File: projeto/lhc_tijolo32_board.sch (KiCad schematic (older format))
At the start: 47 parts, among them J1 USB_C_Receptacle_USB2.0, J2 OLED, J3 JTAG 10pin Connector, J4 Conn_01x20_Male, Q1 MMBT3904, Q2 MMBT3904, SW1 SW_Push, SW2 SW_Push, U1 AMS1117-3.3, U2 CH340G, U3 ESP32-WROOM-32D, Y1 12MHz 10ppm, Y2 32k 20ppm

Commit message: Changed from Sparkfun to Adafruit Feather layout
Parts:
- removed B1: ESP32_THING_W_ANT_KEEPOUT, Boards:ESP32_THING, symbol SparkFun-Boards:ESP32_THING_W_ANT_KEEPOUT
- removed J1: USB_C_Receptacle_USB2.0, Connector_USB:USB_C_Receptacle_Palconn_UTC16-G, symbol Connector:USB_C_Receptacle_USB2.0
- removed J4: Conn_01x20_Male, Connector_PinHeader_2.54mm:PinHeader_1x20_P2.54mm_Vertical, symbol Connector:Conn_01x20_Male
- removed R10, R11: 0R, Resistor_SMD:R_0603_1608Metric, symbol Device:R_US
- removed R2, R3: 5k1R, Resistor_SMD:R_0603_1608Metric, symbol Device:R_US
- removed U1: AMS1117-3.3, Package_TO_SOT_SMD:SOT-223-3_TabPin2, symbol Regulator_Linear:AMS1117-3.3
- added A1: Adafruit_Feather_Generic, Module:Adafruit_Feather, symbol MCU_Module:Adafruit_Feather_Generic
- added J1: USB_A, Connector_USB:USB_A_CNCTech_1001-011-01101_Horizontal, symbol Connector:USB_A
- added J4, J5: CONN_06POLAR, MOLEX-1X6, symbol SparkFun-Connectors:CONN_06POLAR
- added U1: AP2112K-3.3, Package_TO_SOT_SMD:SOT-23-5, symbol Regulator_Linear:AP2112K-3.3
- C10: symbol Device:CP1_Small -> lhc_tijolo32_board-rescue:CP1_Small-Device
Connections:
- wire segments 252 -> 231
- no-connect marks 7 -> 5
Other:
- moved on the sheet: C9, F1

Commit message: Layout updated and added new 3d images
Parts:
- removed R12, R13: 0R, Resistor_SMD:R_0603_1608Metric, symbol Device:R_US
- added C17, C19: 100nF, Capacitor_SMD:C_0603_1608Metric, symbol Device:C_Small
- added C18: 1uF, Capacitor_SMD:C_0603_1608Metric, symbol Device:C_Small
- added U4: AP2112K-3.3, Package_TO_SOT_SMD:SOT-23-5, symbol Regulator_Linear:AP2112K-3.3
- C9: value 100nF -> 1uF
- J4, J5: footprint MOLEX-1X6 -> Connector_PinSocket_2.54mm:PinSocket_1x06_P2.54mm_Vertical
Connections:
- wire segments 231 -> 254
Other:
- moved on the sheet: C11, F1, J1, U2

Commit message: Layout updated
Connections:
- net labels removed: IO16, IO17
- wire segments 254 -> 255
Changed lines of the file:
@@
 IO15-MTDO
 Text GLabel 7950 2350 2    50   BiDi ~ 0
-IO16
+SDA
 Text GLabel 7950 2450 2    50   BiDi ~ 0
-IO17
+SCL
 Text GLabel 7950 2550 2    50   BiDi ~ 0
 IO18
@@
 Text GLabel 9400 2750 0    50   BiDi ~ 0
 IO26
-Text GLabel 9400 2850 0    50   BiDi ~ 0
+Text GLabel 10600 2150 2    50   BiDi ~ 0
 IO27
 Text GLabel 10600 1750 2    50   Input ~ 0
@@
 Wire Wire Line
 	2450 7000 2450 7100
+Wire Wire Line
+	10500 2150 10600 2150
 $EndSCHEMATC

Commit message: Layout improved
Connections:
- wire segments 255 -> 253
- no-connect marks 5 -> 7
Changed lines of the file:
@@
 Wire Notes Line
 	6350 3200 4750 3200
-Text GLabel 10600 2350 2    50   BiDi ~ 0
-IO32-32kXP
-Text GLabel 10600 2450 2    50   Input ~ 0
-IO33-32kXN
 Text GLabel 10600 2550 2    50   Input ~ 0
 IO34
@@
 Text GLabel 10600 1750 2    50   Input ~ 0
 ESP_RST
-Text GLabel 9400 2250 0    50   Input ~ 0
+Text GLabel 9400 1950 0    50   Input ~ 0
 IO21
 Text GLabel 9400 3150 0    50   Input ~ 0
@@
 Text GLabel 9400 3050 0    50   Input ~ 0
 ESP_RX
-Text GLabel 9400 2350 0    50   Input ~ 0
-IO22
+Text GLabel 9400 2050 0    50   Input ~ 0
+IO19
+Text GLabel 9800 1250 0    50   Input ~ 0
+IO23
 Text GLabel 9400 2150 0    50   Input ~ 0
-IO19
-Text GLabel 9400 2450 0    50   Input ~ 0
-IO23
-Text GLabel 9400 2050 0    50   Input ~ 0
 IO18
-Text GLabel 9400 1950 0    50   Input ~ 0
+Text GLabel 9400 2250 0    50   Input ~ 0
 IO5
 Text GLabel 9400 1750 0    50   Input ~ 0
@@
 Text GLabel 10600 2050 2    50   Input ~ 0
 ESP_BOOT
-Text GLabel 9400 1850 0    50   Input ~ 0
+Text GLabel 9400 2350 0    50   Input ~ 0
 IO4
 Text GLabel 9400 3350 0    50   Input ~ 0
@@
 	1    0    0    -1
 $EndComp
-Text GLabel 10600 2750 2    50   Input ~ 0
+Text GLabel 10600 2350 2    50   Input ~ 0
 SVP
-Text GLabel 10600 2850 2    50   Input ~ 0
+Text GLabel 10600 2450 2    50   Input ~ 0
 SVN
 $Comp
@@
 	9400 2350 9500 2350
 Wire Wire Line
-	9400 2450 9500 2450
-Wire Wire Line
 	10500 2350 10600 2350
 Wire Wire Line
@@
 	10500 2650 10600 2650
 Wire Wire Line
-	10500 2750 10600 2750
-Wire Wire Line
-	10500 2850 10600 2850
-Wire Wire Line
 	9400 2650 9500 2650
 Wire Wire Line
 	9400 2750 9500 2750
-Wire Wire Line
-	9400 2850 9500 2850
 Wire Wire Line
 	10000 3950 10000 3850
@@
 Wire Wire Line
 	10500 2150 10600 2150
+Text GLabel 9400 1850 0    50   Input ~ 0
+IO22
+Wire Wire Line
+	9800 1250 9900 1250
+Wire Wire Line
+	9900 1250 9900 1350
+NoConn ~ 9500 2450
+NoConn ~ 9500 2850
 $EndSCHEMATC

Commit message: Layout LIVE
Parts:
- JP1, JP2: footprint Jumper:SolderJumper-3_P1.3mm_Bridged12_Pad1.0x1.5mm_NumberLabels -> Jumper:SolderJumper-3_P1.3mm_Open_Pad1.0x1.5mm_NumberLabels; symbol Jumper:SolderJumper_3_Bridged12 -> Jumper:SolderJumper_3_Open
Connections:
- no-connect marks 7 -> 9
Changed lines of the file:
@@
 SDA
 $Comp
-L Jumper:SolderJumper_3_Bridged12 JP2
+L Jumper:SolderJumper_3_Open JP2
 U 1 1 5F71E23B
 P 3800 3850
 F 0 "JP2" H 3800 4055 50  0000 C CNN
 F 1 "P1" H 3800 3964 50  0000 C CNN
-F 2 "Jumper:SolderJumper-3_P1.3mm_Bridged12_Pad1.0x1.5mm_NumberLabels" H 3800 3850 50  0001 C CNN
+F 2 "Jumper:SolderJumper-3_P1.3mm_Open_Pad1.0x1.5mm_NumberLabels" H 3800 3850 50  0001 C CNN
 F 3 "~" H 3800 3850 50  0001 C CNN
 	1    3800 3850
@@
 $EndComp
 $Comp
-L Jumper:SolderJumper_3_Bridged12 JP1
+L Jumper:SolderJumper_3_Open JP1
 U 1 1 5F71F2AF
 P 3100 3850
 F 0 "JP1" H 3100 4055 50  0000 C CNN
 F 1 "P2" H 3100 3964 50  0000 C CNN
-F 2 "Jumper:SolderJumper-3_P1.3mm_Bridged12_Pad1.0x1.5mm_NumberLabels" H 3100 3850 50  0001 C CNN
+F 2 "Jumper:SolderJumper-3_P1.3mm_Open_Pad1.0x1.5mm_NumberLabels" H 3100 3850 50  0001 C CNN
 F 3 "~" H 3100 3850 50  0001 C CNN
 	1    3100 3850
@@
 Text GLabel 10600 2650 2    50   Input ~ 0
 IO35
-Text GLabel 9400 2650 0    50   BiDi ~ 0
+Text GLabel 10600 2750 2    50   BiDi ~ 0
 IO25
-Text GLabel 9400 2750 0    50   BiDi ~ 0
+Text GLabel 10600 2850 2    50   BiDi ~ 0
 IO26
 Text GLabel 10600 2150 2    50   BiDi ~ 0
@@
 	10500 2650 10600 2650
 Wire Wire Line
-	9400 2650 9500 2650
-Wire Wire Line
-	9400 2750 9500 2750
-Wire Wire Line
 	10000 3950 10000 3850
 $Comp
@@
 NoConn ~ 9500 2450
 NoConn ~ 9500 2850
+Wire Wire Line
+	10500 2750 10600 2750
+Wire Wire Line
+	10500 2850 10600 2850
+NoConn ~ 9500 2750
+NoConn ~ 9500 2650
 $EndSCHEMATC

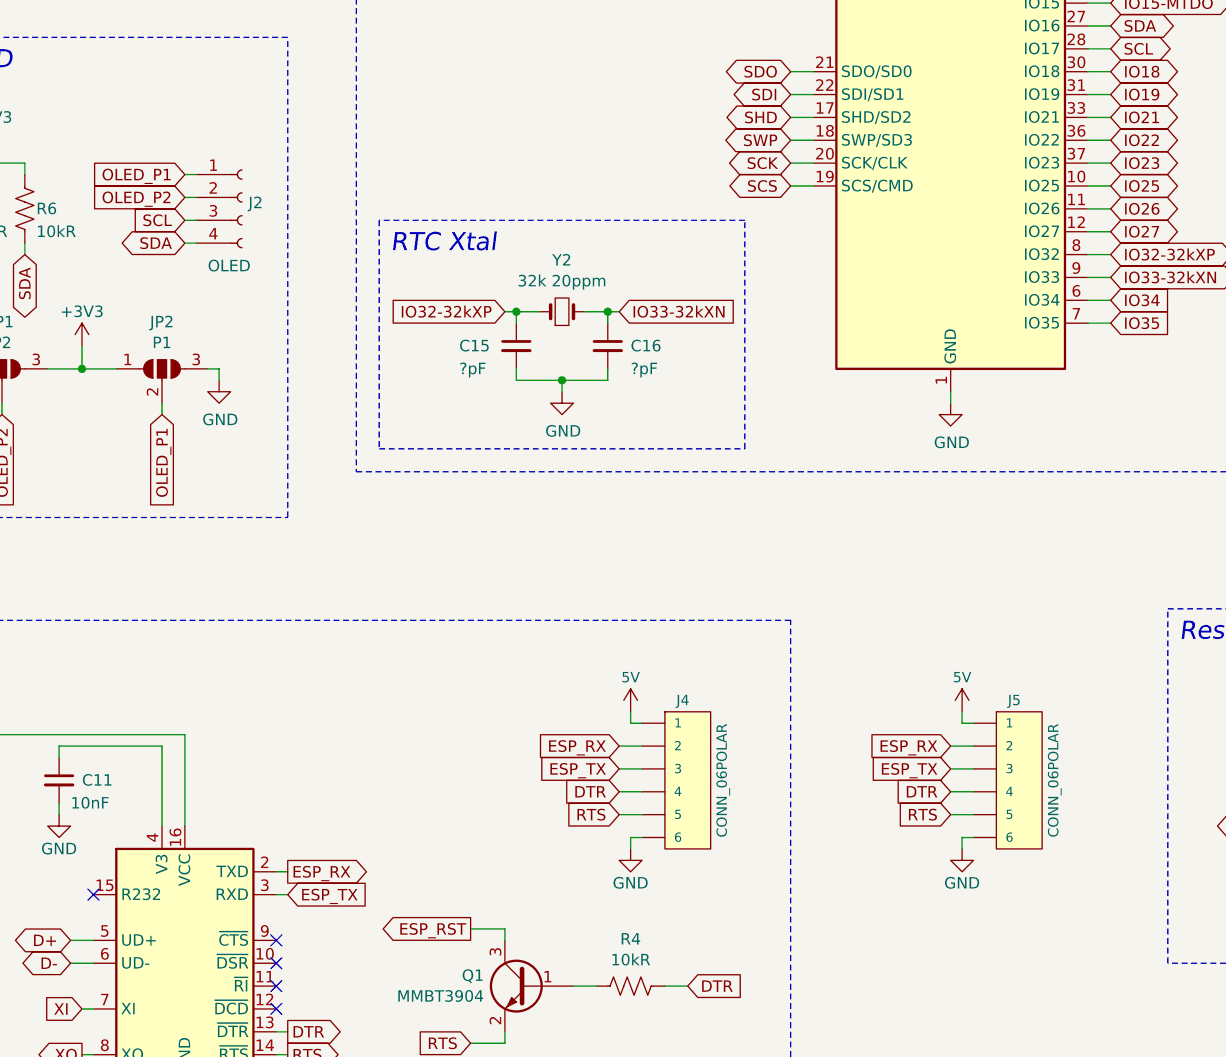
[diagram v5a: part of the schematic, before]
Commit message: Updated on some labels, footprints and symbols
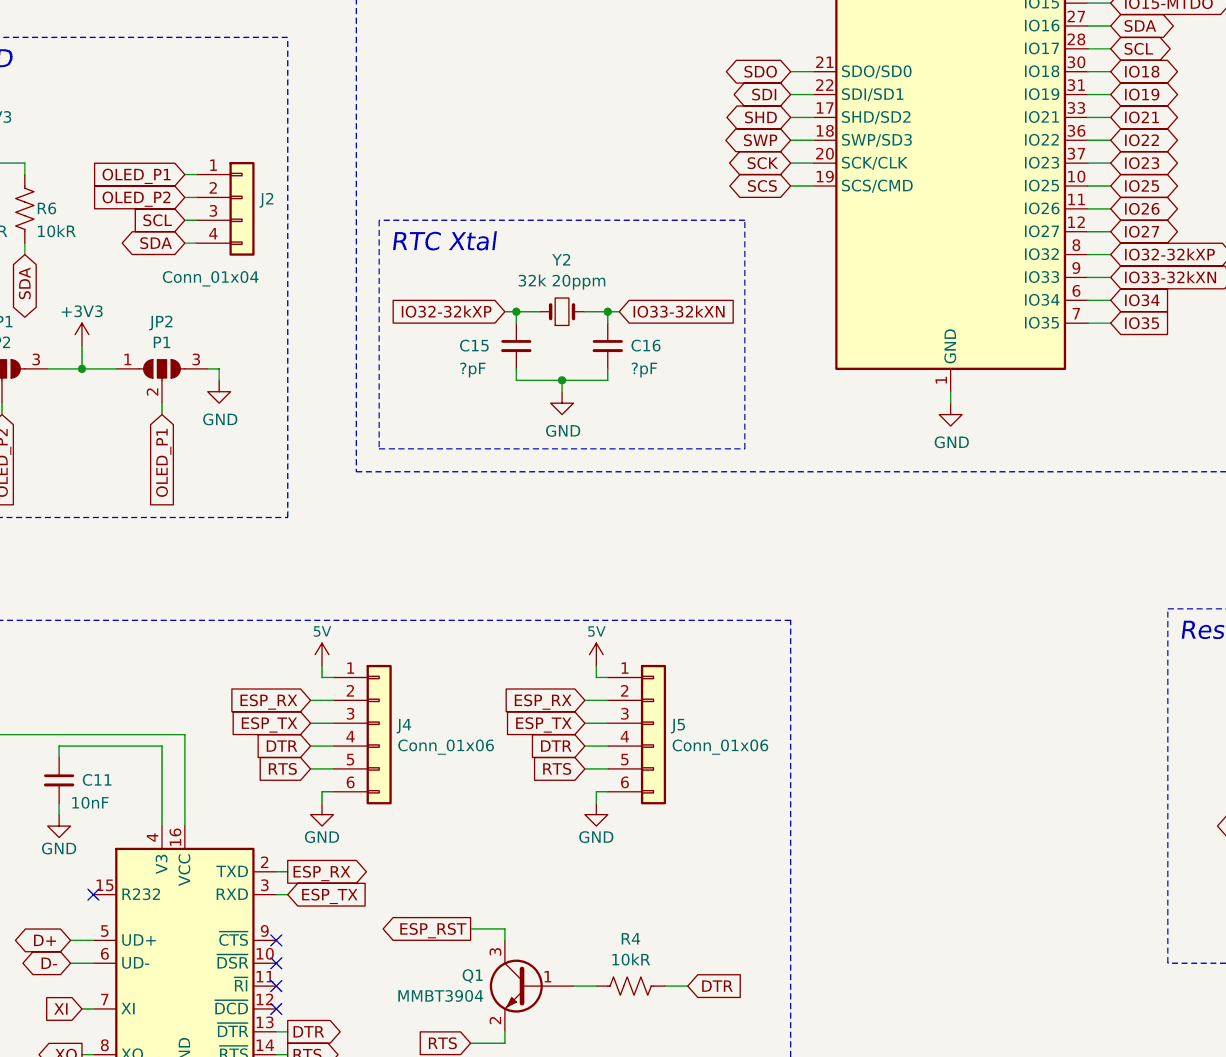
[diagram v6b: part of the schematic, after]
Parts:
- removed J2: OLED, Connector_PinHeader_2.54mm:PinHeader_1x04_P2.54mm_Vertical, symbol Connector:Conn_01x04_Female
- removed J4, J5: CONN_06POLAR, Connector_PinSocket_2.54mm:PinSocket_1x06_P2.54mm_Vertical, symbol SparkFun-Connectors:CONN_06POLAR
- added J2: Conn_01x04, Connector_PinSocket_2.54mm:PinSocket_1x04_P2.54mm_Vertical, symbol Connector_Generic:Conn_01x04
- added J4, J5: Conn_01x06, Connector_PinSocket_2.54mm:PinSocket_1x06_P2.54mm_Vertical, symbol Connector_Generic:Conn_01x06
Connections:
- net 5V: now also J4.1 (Pin_1), J5.1 (Pin_1)
- net DTR: now also J4.4 (Pin_4), J5.4 (Pin_4)
- net ESP_RX: now also J4.2 (Pin_2), J5.2 (Pin_2)
- net ESP_TX: now also J4.3 (Pin_3), J5.3 (Pin_3)
- net GND: now also J4.6 (Pin_6), J5.6 (Pin_6)
- net OLED_P1: now also J2.1 (Pin_1)
- net OLED_P2: now also J2.2 (Pin_2)
- net RTS: now also J4.5 (Pin_5), J5.5 (Pin_5)
- net SCL: now also J2.3 (Pin_3)
- net SDA: now also J2.4 (Pin_4)
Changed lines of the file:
@@
 $EndComp
 $Comp
-L Connector:Conn_01x04_Female J2
-U 1 1 5F4C7D74
-P 4150 3100
-F 0 "J2" H 4178 3076 50  0000 L CNN
-F 1 "OLED" H 4000 2800 50  0000 L CNN
-F 2 "Connector_PinHeader_2.54mm:PinHeader_1x04_P2.54mm_Vertical" H 4150 3100 50  0001 C CNN
-F 3 "~" H 4150 3100 50  0001 C CNN
-	1    4150 3100
-	1    0    0    -1
-$EndComp
-$Comp
-L SparkFun-PowerSymbols:5V #SUPPLY0101
+L lhc_tijolo32_board-rescue:5V-SparkFun-PowerSymbols #SUPPLY0101
 U 1 1 5F4CA7F8
 P 1550 6350
@@
 $EndComp
 $Comp
-L SparkFun-PowerSymbols:5V #SUPPLY0102
+L lhc_tijolo32_board-rescue:5V-SparkFun-PowerSymbols #SUPPLY0102
 U 1 1 5F4EB545
 P 1250 1050
@@
 SCL
 $Comp
-L SparkFun-PowerSymbols:5V #SUPPLY02
+L lhc_tijolo32_board-rescue:5V-SparkFun-PowerSymbols #SUPPLY02
 U 1 1 5F88471D
 P 10300 1050
@@
 	10000 3950 10000 3850
 $Comp
-L SparkFun-Connectors:CONN_06POLAR J4
-U 1 1 60537E72
-P 6000 5400
-F 0 "J4" H 5950 5300 45  0000 R CNN
-F 1 "CONN_06POLAR" V 5750 5900 45  0000 R CNN
-F 2 "Connector_PinSocket_2.54mm:PinSocket_1x06_P2.54mm_Vertical" H 6000 6100 20  0001 C CNN
-F 3 "" H 6000 5400 50  0001 C CNN
-F 4 "XXX-00000" H 5772 5734 60  0001 R CNN "Field4"
-	1    6000 5400
-	-1   0    0    1
-$EndComp
-$Comp
-L SparkFun-PowerSymbols:5V #SUPPLY0103
+L lhc_tijolo32_board-rescue:5V-SparkFun-PowerSymbols #SUPPLY0103
 U 1 1 6054C50E
-P 5850 5350
-F 0 "#SUPPLY0103" H 5900 5350 45  0001 L BNN
-F 1 "5V" H 5850 5500 45  0000 C CNN
-F 2 "XXX-00000" H 5850 5531 60  0001 C CNN
-F 3 "" H 5850 5350 60  0001 C CNN
-	1    5850 5350
+P 4500 5150
+F 0 "#SUPPLY0103" H 4550 5150 45  0001 L BNN
+F 1 "5V" H 4500 5300 45  0000 C CNN
+F 2 "XXX-00000" H 4500 5331 60  0001 C CNN
+F 3 "" H 4500 5150 60  0001 C CNN
+	1    4500 5150
 	1    0    0    -1
 $EndComp
@@
 L power:GND #PWR0103
 U 1 1 6055020E
-P 5850 5950
-F 0 "#PWR0103" H 5850 5700 50  0001 C CNN
-F 1 "GND" H 5850 5800 50  0000 C CNN
-F 2 "" H 5850 5950 50  0001 C CNN
-F 3 "" H 5850 5950 50  0001 C CNN
-	1    5850 5950
-	1    0    0    -1
-$EndComp
-Wire Wire Line
-	5850 5350 5850 5400
-Wire Wire Line
-	5850 5400 5900 5400
-Wire Wire Line
-	5900 5900 5850 5900
-Wire Wire Line
-	5850 5900 5850 5950
-Text GLabel 5800 5500 0    50   Input ~ 0
+P 4500 5750
+F 0 "#PWR0103" H 4500 5500 50  0001 C CNN
+F 1 "GND" H 4500 5600 50  0000 C CNN
+F 2 "" H 4500 5750 50  0001 C CNN
+F 3 "" H 4500 5750 50  0001 C CNN
+	1    4500 5750
+	1    0    0    -1
+$EndComp
+Wire Wire Line
+	4500 5150 4500 5200
+Wire Wire Line
+	4500 5200 4550 5200
+Wire Wire Line
+	4550 5700 4500 5700
+Wire Wire Line
+	4500 5700 4500 5750
+Text GLabel 4450 5300 0    50   Input ~ 0
 ESP_RX
-Text GLabel 5800 5600 0    50   Input ~ 0
+Text GLabel 4450 5400 0    50   Input ~ 0
 ESP_TX
-Text GLabel 5800 5700 0    50   Input ~ 0
+Text GLabel 4450 5500 0    50   Input ~ 0
 DTR
-Text GLabel 5800 5800 0    50   Input ~ 0
+Text GLabel 4450 5600 0    50   Input ~ 0
 RTS
 Wire Wire Line
-	5800 5500 5900 5500
-Wire Wire Line
-	5800 5600 5900 5600
-Wire Wire Line
-	5800 5700 5900 5700
-Wire Wire Line
-	5800 5800 5900 5800
-$Comp
-L SparkFun-Connectors:CONN_06POLAR J5
-U 1 1 605BC0A5
-P 7450 5400
-F 0 "J5" H 7400 5300 45  0000 R CNN
-F 1 "CONN_06POLAR" V 7200 5900 45  0000 R CNN
-F 2 "Connector_PinSocket_2.54mm:PinSocket_1x06_P2.54mm_Vertical" H 7450 6100 20  0001 C CNN
-F 3 "" H 7450 5400 50  0001 C CNN
-F 4 "XXX-00000" H 7222 5734 60  0001 R CNN "Field4"
-	1    7450 5400
-	-1   0    0    1
-$EndComp
-$Comp
-L SparkFun-PowerSymbols:5V #SUPPLY0104
+	4450 5300 4550 5300
+Wire Wire Line
+	4450 5400 4550 5400
+Wire Wire Line
+	4450 5500 4550 5500
+Wire Wire Line
+	4450 5600 4550 5600
+$Comp
+L lhc_tijolo32_board-rescue:5V-SparkFun-PowerSymbols #SUPPLY0104
 U 1 1 605BC0AB
-P 7300 5350
-F 0 "#SUPPLY0104" H 7350 5350 45  0001 L BNN
-F 1 "5V" H 7300 5500 45  0000 C CNN
-F 2 "XXX-00000" H 7300 5531 60  0001 C CNN
-F 3 "" H 7300 5350 60  0001 C CNN
-	1    7300 5350
+P 5700 5150
+F 0 "#SUPPLY0104" H 5750 5150 45  0001 L BNN
+F 1 "5V" H 5700 5300 45  0000 C CNN
+F 2 "XXX-00000" H 5700 5331 60  0001 C CNN
+F 3 "" H 5700 5150 60  0001 C CNN
+	1    5700 5150
 	1    0    0    -1
 $EndComp
@@
 L power:GND #PWR0129
 U 1 1 605BC0B1
-P 7300 5950
-F 0 "#PWR0129" H 7300 5700 50  0001 C CNN
-F 1 "GND" H 7300 5800 50  0000 C CNN
-F 2 "" H 7300 5950 50  0001 C CNN
-F 3 "" H 7300 5950 50  0001 C CNN
-	1    7300 5950
-	1    0    0    -1
-$EndComp
-Wire Wire Line
-	7300 5350 7300 5400
-Wire Wire Line
-	7300 5400 7350 5400
-Wire Wire Line
-	7350 5900 7300 5900
-Wire Wire Line
-	7300 5900 7300 5950
-Text GLabel 7250 5500 0    50   Input ~ 0
+P 5700 5750
+F 0 "#PWR0129" H 5700 5500 50  0001 C CNN
+F 1 "GND" H 5700 5600 50  0000 C CNN
+F 2 "" H 5700 5750 50  0001 C CNN
+F 3 "" H 5700 5750 50  0001 C CNN
+	1    5700 5750
+	1    0    0    -1
+$EndComp
+Wire Wire Line
+	5700 5150 5700 5200
+Wire Wire Line
+	5700 5200 5750 5200
+Wire Wire Line
+	5750 5700 5700 5700
+Wire Wire Line
+	5700 5700 5700 5750
+Text GLabel 5650 5300 0    50   Input ~ 0
 ESP_RX
-Text GLabel 7250 5600 0    50   Input ~ 0
+Text GLabel 5650 5400 0    50   Input ~ 0
 ESP_TX
-Text GLabel 7250 5700 0    50   Input ~ 0
+Text GLabel 5650 5500 0    50   Input ~ 0
 DTR
-Text GLabel 7250 5800 0    50   Input ~ 0
+Text GLabel 5650 5600 0    50   Input ~ 0
 RTS
 Wire Wire Line
-	7250 5500 7350 5500
-Wire Wire Line
-	7250 5600 7350 5600
-Wire Wire Line
-	7250 5700 7350 5700
-Wire Wire Line
-	7250 5800 7350 5800
+	5650 5300 5750 5300
+Wire Wire Line
+	5650 5400 5750 5400
+Wire Wire Line
+	5650 5500 5750 5500
+Wire Wire Line
+	5650 5600 5750 5600
 Wire Wire Line
 	1000 5450 1150 5450
@@
 	1000 5450 1000 5400
 $Comp
-L SparkFun-PowerSymbols:5V #SUPPLY0105
+L lhc_tijolo32_board-rescue:5V-SparkFun-PowerSymbols #SUPPLY0105
 U 1 1 60055CEE
 P 1000 5400
@@
 NoConn ~ 9500 2750
 NoConn ~ 9500 2650
+$Comp
+L Connector_Generic:Conn_01x06 J4
+U 1 1 60E6BCFF
+P 4750 5400
+F 0 "J4" H 4830 5392 50  0000 L CNN
+F 1 "Conn_01x06" H 4830 5301 50  0000 L CNN
+F 2 "Connector_PinSocket_2.54mm:PinSocket_1x06_P2.54mm_Vertical" H 4750 5400 50  0001 C CNN
+F 3 "~" H 4750 5400 50  0001 C CNN
+	1    4750 5400
+	1    0    0    -1
+$EndComp
+$Comp
+L Connector_Generic:Conn_01x06 J5
+U 1 1 60E71DE0
+P 5950 5400
+F 0 "J5" H 6030 5392 50  0000 L CNN
+F 1 "Conn_01x06" H 6030 5301 50  0000 L CNN
+F 2 "Connector_PinSocket_2.54mm:PinSocket_1x06_P2.54mm_Vertical" H 5950 5400 50  0001 C CNN
+F 3 "~" H 5950 5400 50  0001 C CNN
+	1    5950 5400
+	1    0    0    -1
+$EndComp
+$Comp
+L Connector_Generic:Conn_01x04 J2
+U 1 1 60EE69F4
+P 4150 3100
+F 0 "J2" H 4230 3092 50  0000 L CNN
+F 1 "Conn_01x04" H 3800 2750 50  0000 L CNN
+F 2 "Connector_PinSocket_2.54mm:PinSocket_1x04_P2.54mm_Vertical" H 4150 3100 50  0001 C CNN
+F 3 "~" H 4150 3100 50  0001 C CNN
+	1    4150 3100
+	1    0    0    -1
+$EndComp
 $EndSCHEMATC

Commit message: Componentes 3D adicionados
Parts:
- A1: symbol MCU_Module:Adafruit_Feather_Generic -> lhc_tijolo32_board-rescue:Adafruit_Feather_Generic-MCU_Module
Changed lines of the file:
@@
 $EndComp
 $Comp
-L MCU_Module:Adafruit_Feather_Generic A1
+L lhc_tijolo32_board-rescue:Adafruit_Feather_Generic-MCU_Module A1
 U 1 1 60103BE5
 P 10000 2550
